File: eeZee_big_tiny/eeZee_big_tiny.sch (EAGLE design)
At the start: 10 parts, among them IC1 ATtiny2313

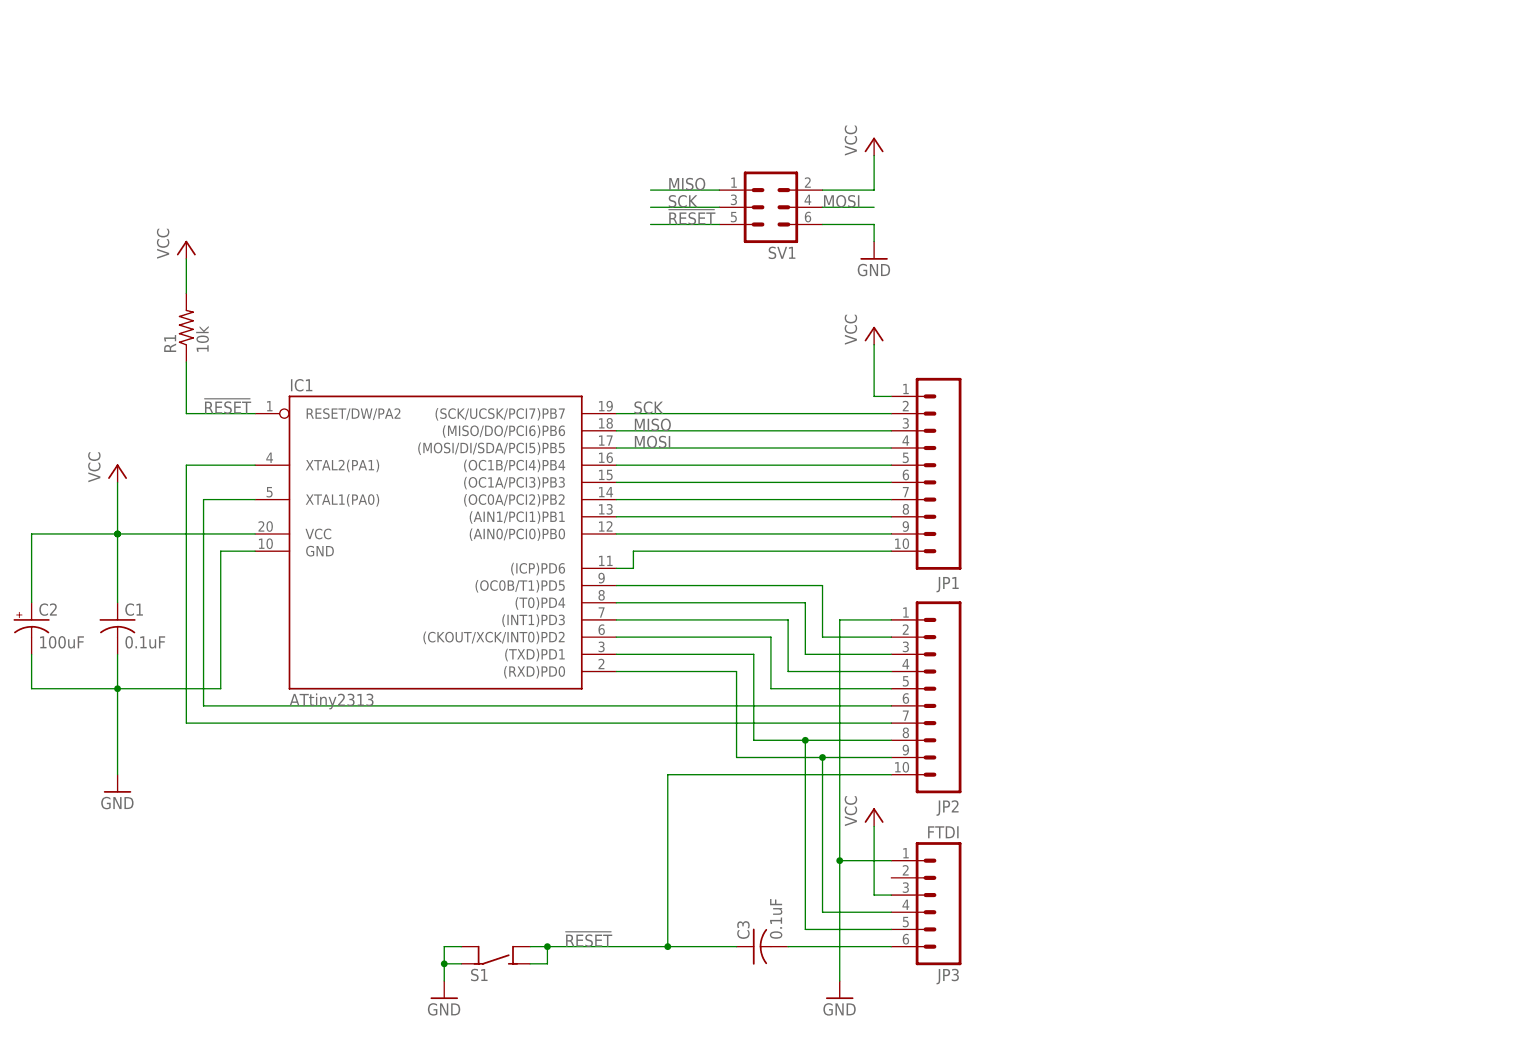
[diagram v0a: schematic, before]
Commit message: Tweaks to big cap, routing
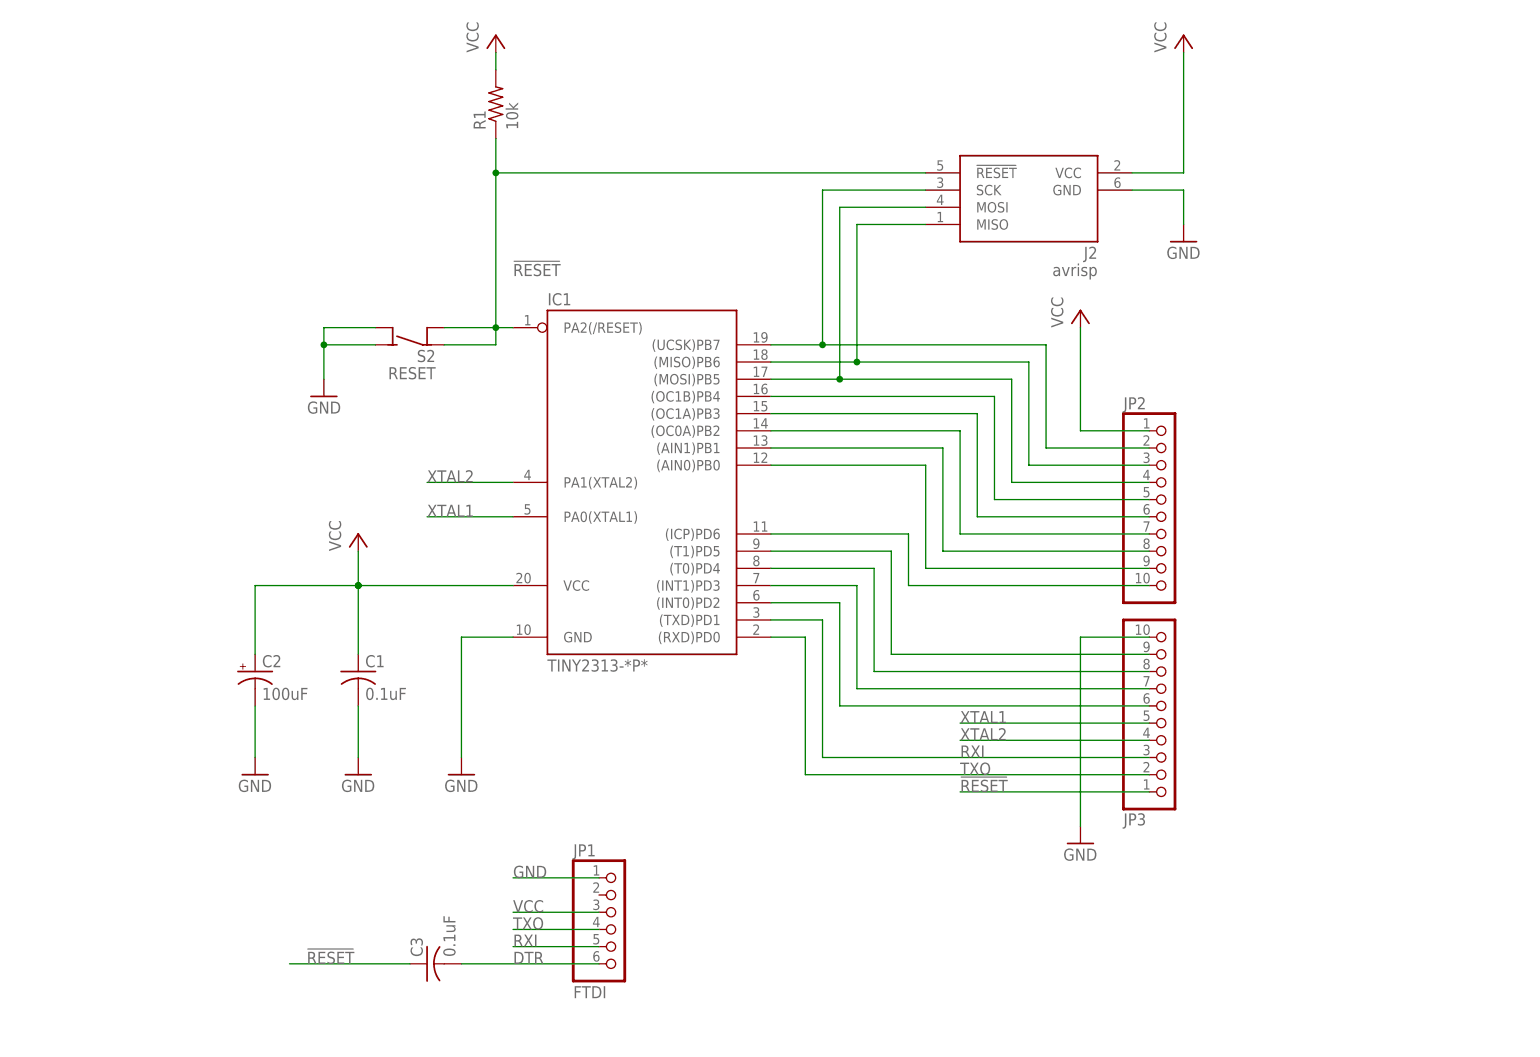
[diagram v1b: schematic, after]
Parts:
- removed S1: (no value), mes_electromech:SPST4
- removed SV1: (no value), con-lstb:MA03-2
- added J2: avrisp, ads4:AVRISP6
- added S2: RESET, mes_electromech:SPST4
- C1, C3: BOM (none) -> EXCLUDE; PARTNO (none) -> 0603YC104KAT2A
- C2: device rcl:CPOL-USSMCC -> rcl:CPOL-USSMCB; BOM (none) -> EXCLUDE; PARTNO (none) -> MCTT21X106M6R3CT
- IC1: value ATtiny2313 -> TINY2313-*P*; device avr:ATTINY2313-20P -> avr-7:TINY2313-*P*
- JP1: value M100.1 -> FTDI; device SparkFun:M100.1 -> pinhead-2:PINHD-1X06_2.54-S
- JP2: value M100.1 -> (none); device SparkFun:M100.1 -> pinhead-2:PINHD-1X10_2.54-S
- JP3: value FTDI -> (none); device SparkFun:M06SIP -> pinhead-2:PINHD-1X10_2.54-S
- R1: PARTNO (none) -> ERJ-3GEYJ103V
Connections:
- removed net MISO: IC1.(MISO/DO/PCI6)PB6, JP1.3, SV1.1
- removed net MOSI: IC1.(MOSI/DI/SDA/PCI5)PB5, JP1.4, SV1.4
- removed net N$1: C3.2, JP3.6
- removed net N$16: IC1.(INT1)PD3, JP2.4
- removed net N$17: IC1.(CKOUT/XCK/INT0)PD2, JP2.5
- removed net N$18: IC1.(TXD)PD1, JP2.8, JP3.5
- removed net RX: IC1.(RXD)PD0, JP2.9, JP3.4
- removed net SCK: IC1.(SCK/UCSK/PCI7)PB7, JP1.2, SV1.3
- new net DTR: C3.2, JP1.6
- new net N$4: IC1.(UCSK)PB7, J2.SCK, JP2.2
- new net N$6: IC1.(INT0)PD2, JP3.6
- new net N$7: IC1.(INT1)PD3, JP3.7
- new net RXI: IC1.(TXD)PD1, JP1.5, JP3.3
- new net TXO: IC1.(RXD)PD0, JP1.4, JP3.2
- new net XTAL1: IC1.PA0(XTAL1), JP3.5
- new net XTAL2: IC1.PA1(XTAL2), JP3.4
- net !RESET: now also IC1.PA2(/RESET), J2.!RESET, JP3.1, S2.COM@1, S2.COM@2; no longer IC1.RESET/DW/PA2, JP2.10, S1.NO@1, S1.NO@2, SV1.5
- net GND: now also J2.GND, JP1.1, JP3.10, S2.NO@1, S2.NO@2; no longer JP2.1, JP3.1, S1.COM@1, S1.COM@2, SV1.6
- net N$10: now also IC1.(ICP)PD6, JP2.10; no longer IC1.(OC0A/PCI2)PB2, JP1.7
- net N$11: now also IC1.(AIN0)PB0, JP2.9; no longer IC1.(AIN1/PCI1)PB1, JP1.8
- net N$12: now also IC1.(AIN1)PB1, JP2.8; no longer IC1.(AIN0/PCI0)PB0, JP1.9
- net N$13: now also IC1.(OC0A)PB2, JP2.7; no longer IC1.(ICP)PD6, JP1.10
- net N$14: now also IC1.(OC1A)PB3, JP2.6; no longer IC1.(OC0B/T1)PD5, JP2.2
- net N$15: now also IC1.(OC1B)PB4, JP2.5; no longer IC1.(T0)PD4, JP2.3
- net N$2: now also IC1.(MISO)PB6, J2.MISO, JP2.3; no longer IC1.XTAL2(PA1), JP2.7
- net N$3: now also IC1.(MOSI)PB5, J2.MOSI, JP2.4; no longer IC1.XTAL1(PA0), JP2.6
- net N$8: now also IC1.(T0)PD4, JP3.8; no longer IC1.(OC1B/PCI4)PB4, JP1.5
- net N$9: now also IC1.(T1)PD5, JP3.9; no longer IC1.(OC1A/PCI3)PB3, JP1.6
- net VCC: now also J2.VCC, JP1.3, JP2.1; no longer JP1.1, JP3.3, SV1.2
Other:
- moved on the sheet: C1, C2, C3, IC1, R1

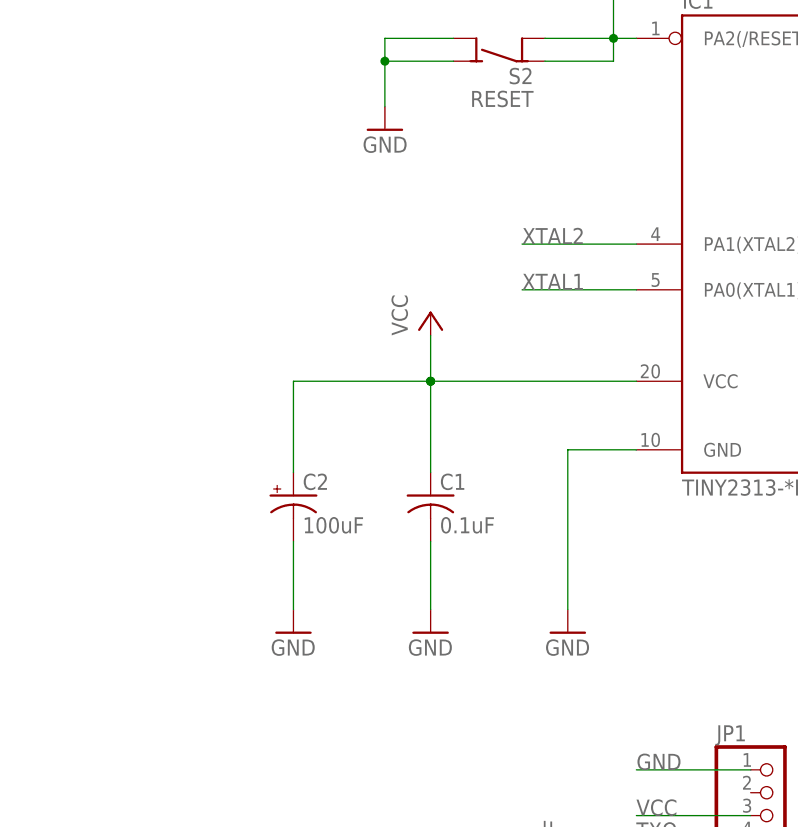
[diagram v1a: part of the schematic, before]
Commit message: Added crystal+caps
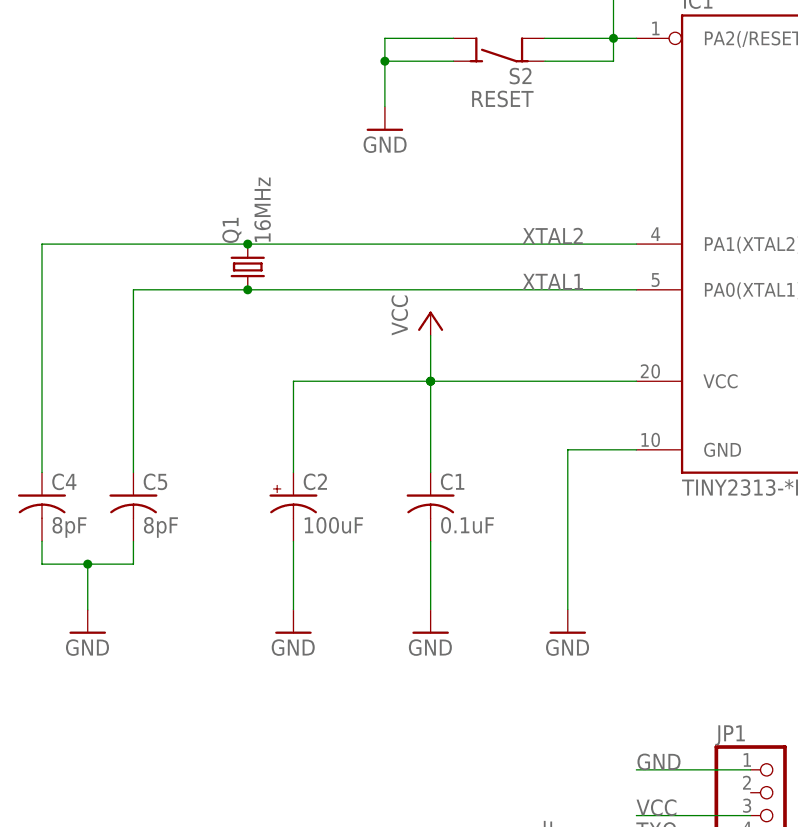
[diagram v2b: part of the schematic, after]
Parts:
- added C4, C5: 8pF, rcl:C-USC0603
- added Q1: 16MHz, mes_crystal:CRYSTALNDK5X3
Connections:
- net GND: now also C4.2, C5.2
- net XTAL1: now also C5.1, Q1.1
- net XTAL2: now also C4.1, Q1.2
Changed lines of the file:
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@@
 <attribute name="PARTNO" value="MCTT21X106M6R3CT"/>
 </part>
+<part name="Q1" library="mes_crystal" deviceset="CRYSTAL" device="NDK5X3" value="16MHz"/>
+<part name="C4" library="rcl" deviceset="C-US" device="C0603" value="8pF">
+<attribute name="BOM" value="EXCLUDE"/>
+<attribute name="PARTNO" value="0603YC104KAT2A"/>
+</part>
+<part name="C5" library="rcl" deviceset="C-US" device="C0603" value="8pF">
+<attribute name="BOM" value="EXCLUDE"/>
+<attribute name="PARTNO" value="0603YC104KAT2A"/>
+</part>
+<part name="GND7" library="supply1" deviceset="GND" device=""/>
 </parts>
 <sheets>
@@
 <attribute name="BOM" value="EXCLUDE" x="58.42" y="76.2" size="1.778" layer="96" display="off"/>
 </instance>
+<instance part="Q1" gate="G$1" x="53.34" y="101.6" rot="R90"/>
+<instance part="C4" gate="G$1" x="30.48" y="76.2">
+<attribute name="PARTNO" value="0603YC104KAT2A" x="30.48" y="76.2" size="1.778" layer="96" display="off"/>
+<attribute name="BOM" value="EXCLUDE" x="30.48" y="76.2" size="1.778" layer="96" display="off"/>
+</instance>
+<instance part="C5" gate="G$1" x="40.64" y="76.2">
+<attribute name="PARTNO" value="0603YC104KAT2A" x="40.64" y="76.2" size="1.778" layer="96" display="off"/>
+<attribute name="BOM" value="EXCLUDE" x="40.64" y="76.2" size="1.778" layer="96" display="off"/>
+</instance>
+<instance part="GND7" gate="1" x="35.56" y="60.96"/>
 </instances>
 <busses>
@@
 <wire x1="109.22" y1="45.72" x2="96.52" y2="45.72" width="0.1524" layer="91"/>
 <label x="96.52" y="45.72" size="1.778" layer="95"/>
+</segment>
+<segment>
+<pinref part="C4" gate="G$1" pin="2"/>
+<wire x1="30.48" y1="71.12" x2="30.48" y2="68.58" width="0.1524" layer="91"/>
+<pinref part="C5" gate="G$1" pin="2"/>
+<wire x1="30.48" y1="68.58" x2="35.56" y2="68.58" width="0.1524" layer="91"/>
+<wire x1="35.56" y1="68.58" x2="40.64" y2="68.58" width="0.1524" layer="91"/>
+<wire x1="40.64" y1="68.58" x2="40.64" y2="71.12" width="0.1524" layer="91"/>
+<wire x1="35.56" y1="68.58" x2="35.56" y2="63.5" width="0.1524" layer="91"/>
+<pinref part="GND7" gate="1" pin="GND"/>
+<junction x="35.56" y="68.58"/>
 </segment>
 </net>
@@
 <segment>
 <pinref part="IC1" gate="G$1" pin="PA1(XTAL2)"/>
-<wire x1="96.52" y1="104.14" x2="83.82" y2="104.14" width="0.1524" layer="91"/>
 <label x="83.82" y="104.14" size="1.778" layer="95"/>
+<pinref part="C4" gate="G$1" pin="1"/>
+<wire x1="96.52" y1="104.14" x2="53.34" y2="104.14" width="0.1524" layer="91"/>
+<wire x1="53.34" y1="104.14" x2="30.48" y2="104.14" width="0.1524" layer="91"/>
+<wire x1="30.48" y1="104.14" x2="30.48" y2="78.74" width="0.1524" layer="91"/>
+<pinref part="Q1" gate="G$1" pin="2"/>
+<junction x="53.34" y="104.14"/>
 </segment>
 <segment>
@@
 <segment>
 <pinref part="IC1" gate="G$1" pin="PA0(XTAL1)"/>
-<wire x1="96.52" y1="99.06" x2="83.82" y2="99.06" width="0.1524" layer="91"/>
 <label x="83.82" y="99.06" size="1.778" layer="95"/>
-</segment>
-<segment>
+<pinref part="C5" gate="G$1" pin="1"/>
+<wire x1="96.52" y1="99.06" x2="53.34" y2="99.06" width="0.1524" layer="91"/>
+<wire x1="53.34" y1="99.06" x2="40.64" y2="99.06" width="0.1524" layer="91"/>
+<wire x1="40.64" y1="99.06" x2="40.64" y2="78.74" width="0.1524" layer="91"/>
+<pinref part="Q1" gate="G$1" pin="1"/>
+<junction x="53.34" y="99.06"/>
+</segment>
+<segment>

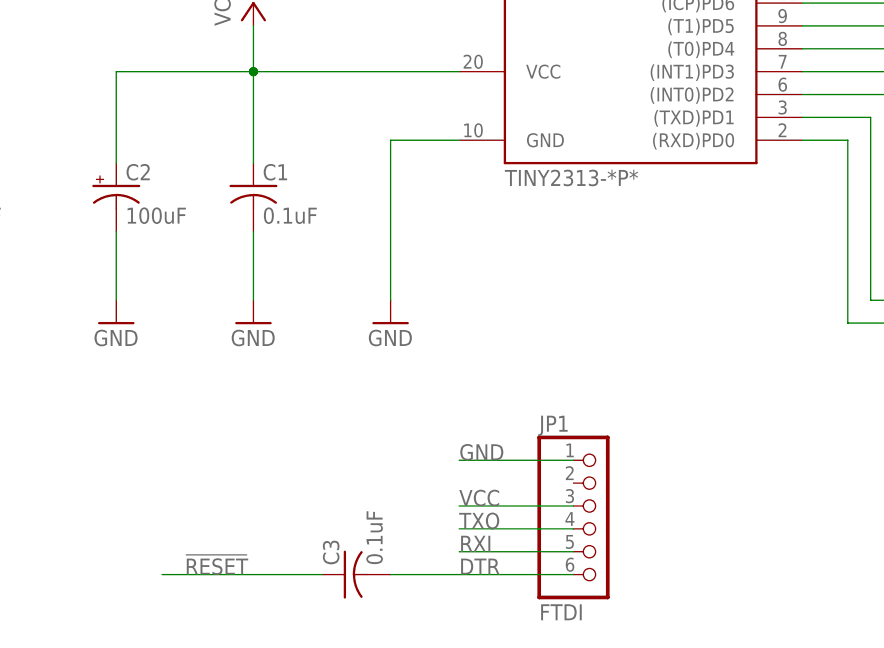
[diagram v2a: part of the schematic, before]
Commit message: Removed FTDI header, revised layout to reduce leading edge clearance on breadboard.
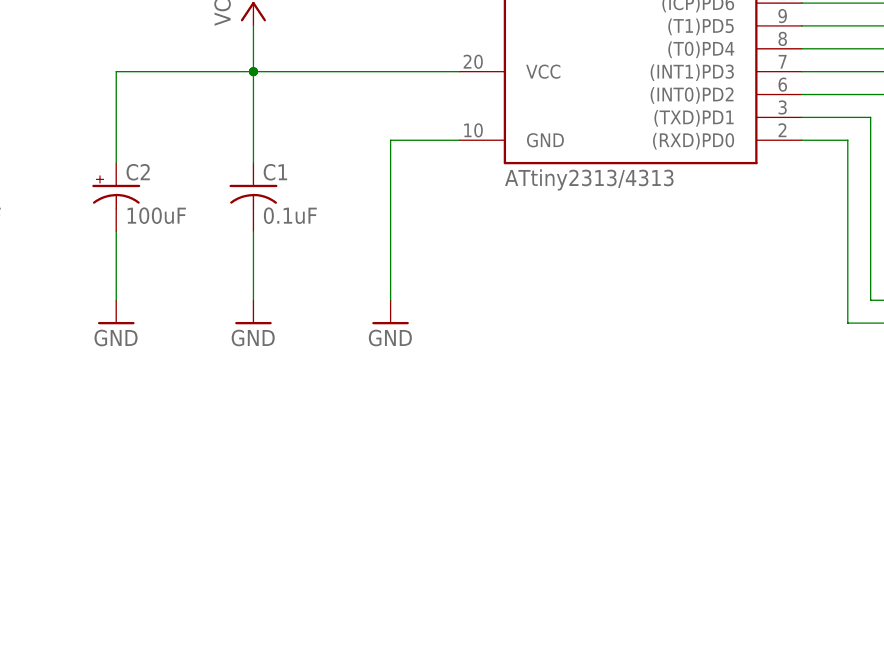
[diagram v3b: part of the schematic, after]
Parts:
- removed C3: 0.1uF, rcl:C-USC0603
- removed JP1: FTDI, pinhead-2:PINHD-1X06_2.54-S
- IC1: value TINY2313-*P* -> ATtiny2313/4313
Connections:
- removed net DTR: C3.2, JP1.6
- net !RESET: no longer C3.1
- net GND: no longer JP1.1
- net RXI: no longer JP1.5
- net TXO: no longer JP1.4
- net VCC: no longer JP1.3
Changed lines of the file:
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@@
 <part name="J2" library="ads4" deviceset="AVRISP6" device="" value="avrisp"/>
 <part name="S2" library="mes_electromech" deviceset="SPST4" device="" value="RESET"/>
-<part name="IC1" library="avr-7" deviceset="TINY2313*" device="-*P*"/>
+<part name="IC1" library="avr-7" deviceset="TINY2313*" device="-*P*" value="ATtiny2313/4313"/>
 <part name="JP3" library="pinhead-2" deviceset="PINHD-1X10" device="_2.54-S"/>
 <part name="JP2" library="pinhead-2" deviceset="PINHD-1X10" device="_2.54-S"/>
-<part name="JP1" library="pinhead-2" deviceset="PINHD-1X06" device="_2.54-S" value="FTDI"/>
 <part name="GND4" library="supply1" deviceset="GND" device=""/>
 <part name="P+4" library="supply1" deviceset="VCC" device=""/>
-<part name="C3" library="rcl" deviceset="C-US" device="C0603" value="0.1uF">
-<attribute name="BOM" value="EXCLUDE"/>
-<attribute name="PARTNO" value="0603YC104KAT2A"/>
-</part>
 <part name="FRAME1" library="mes" deviceset="LETTER_L" device=""/>
 <part name="GND5" library="supply1" deviceset="GND" device=""/>
@@
 <instance part="JP3" gate="A" x="193.04" y="68.58" rot="MR180"/>
 <instance part="JP2" gate="A" x="193.04" y="101.6"/>
-<instance part="JP1" gate="A" x="111.76" y="38.1"/>
 <instance part="GND4" gate="1" x="180.34" y="50.8"/>
 <instance part="P+4" gate="VCC" x="180.34" y="129.54"/>
-<instance part="C3" gate="G$1" x="83.82" y="33.02" rot="R90">
-<attribute name="PARTNO" value="0603YC104KAT2A" x="83.82" y="33.02" size="1.778" layer="96" rot="R90" display="off"/>
-<attribute name="BOM" value="EXCLUDE" x="83.82" y="33.02" size="1.778" layer="96" rot="R90" display="off"/>
-</instance>
 <instance part="FRAME1" gate="G$1" x="248.92" y="185.42" rot="R180"/>
 <instance part="FRAME1" gate="G$2" x="248.92" y="27.94" rot="R180"/>
@@
 <wire x1="180.34" y1="81.28" x2="180.34" y2="53.34" width="0.1524" layer="91"/>
 <pinref part="GND4" gate="1" pin="GND"/>
-</segment>
-<segment>
-<pinref part="JP1" gate="A" pin="1"/>
-<wire x1="109.22" y1="45.72" x2="96.52" y2="45.72" width="0.1524" layer="91"/>
-<label x="96.52" y="45.72" size="1.778" layer="95"/>
 </segment>
 <segment>
@@
 <wire x1="180.34" y1="111.76" x2="180.34" y2="127" width="0.1524" layer="91"/>
 <pinref part="P+4" gate="VCC" pin="VCC"/>
-</segment>
-<segment>
-<pinref part="JP1" gate="A" pin="3"/>
-<wire x1="109.22" y1="40.64" x2="96.52" y2="40.64" width="0.1524" layer="91"/>
-<label x="96.52" y="40.64" size="1.778" layer="95"/>
 </segment>
 </net>
@@
 <label x="162.56" y="58.42" size="1.778" layer="95"/>
 </segment>
-<segment>
-<pinref part="C3" gate="G$1" pin="1"/>
-<wire x1="81.28" y1="33.02" x2="63.5" y2="33.02" width="0.1524" layer="91"/>
-<label x="66.04" y="33.02" size="1.778" layer="95"/>
-</segment>
 </net>
 <net name="N$3" class="0">
@@
 </segment>
 </net>
-<net name="DTR" class="0">
-<segment>
-<pinref part="JP1" gate="A" pin="6"/>
-<wire x1="109.22" y1="33.02" x2="88.9" y2="33.02" width="0.1524" layer="91"/>
-<label x="96.52" y="33.02" size="1.778" layer="95"/>
-<pinref part="C3" gate="G$1" pin="2"/>
-</segment>
-</net>
 <net name="RXI" class="0">
-<segment>
-<pinref part="JP1" gate="A" pin="5"/>
-<wire x1="109.22" y1="35.56" x2="96.52" y2="35.56" width="0.1524" layer="91"/>
-<label x="96.52" y="35.56" size="1.778" layer="95"/>
-</segment>
 <segment>
 <pinref part="JP3" gate="A" pin="3"/>
@@
 <net name="TXO" class="0">
 <segment>
-<pinref part="JP1" gate="A" pin="4"/>
-<wire x1="109.22" y1="38.1" x2="96.52" y2="38.1" width="0.1524" layer="91"/>
-<label x="96.52" y="38.1" size="1.778" layer="95"/>
-</segment>
-<segment>
 <pinref part="IC1" gate="G$1" pin="(RXD)PD0"/>
